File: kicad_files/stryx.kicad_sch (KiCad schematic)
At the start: 24 parts, among them M1 12V 250 RPM, M2 12V 250 RPM, U1 LM317_TO-220, U2 NUCLEO-L432KC, U3 TB6612FNG-Module, U4 HC-SR04

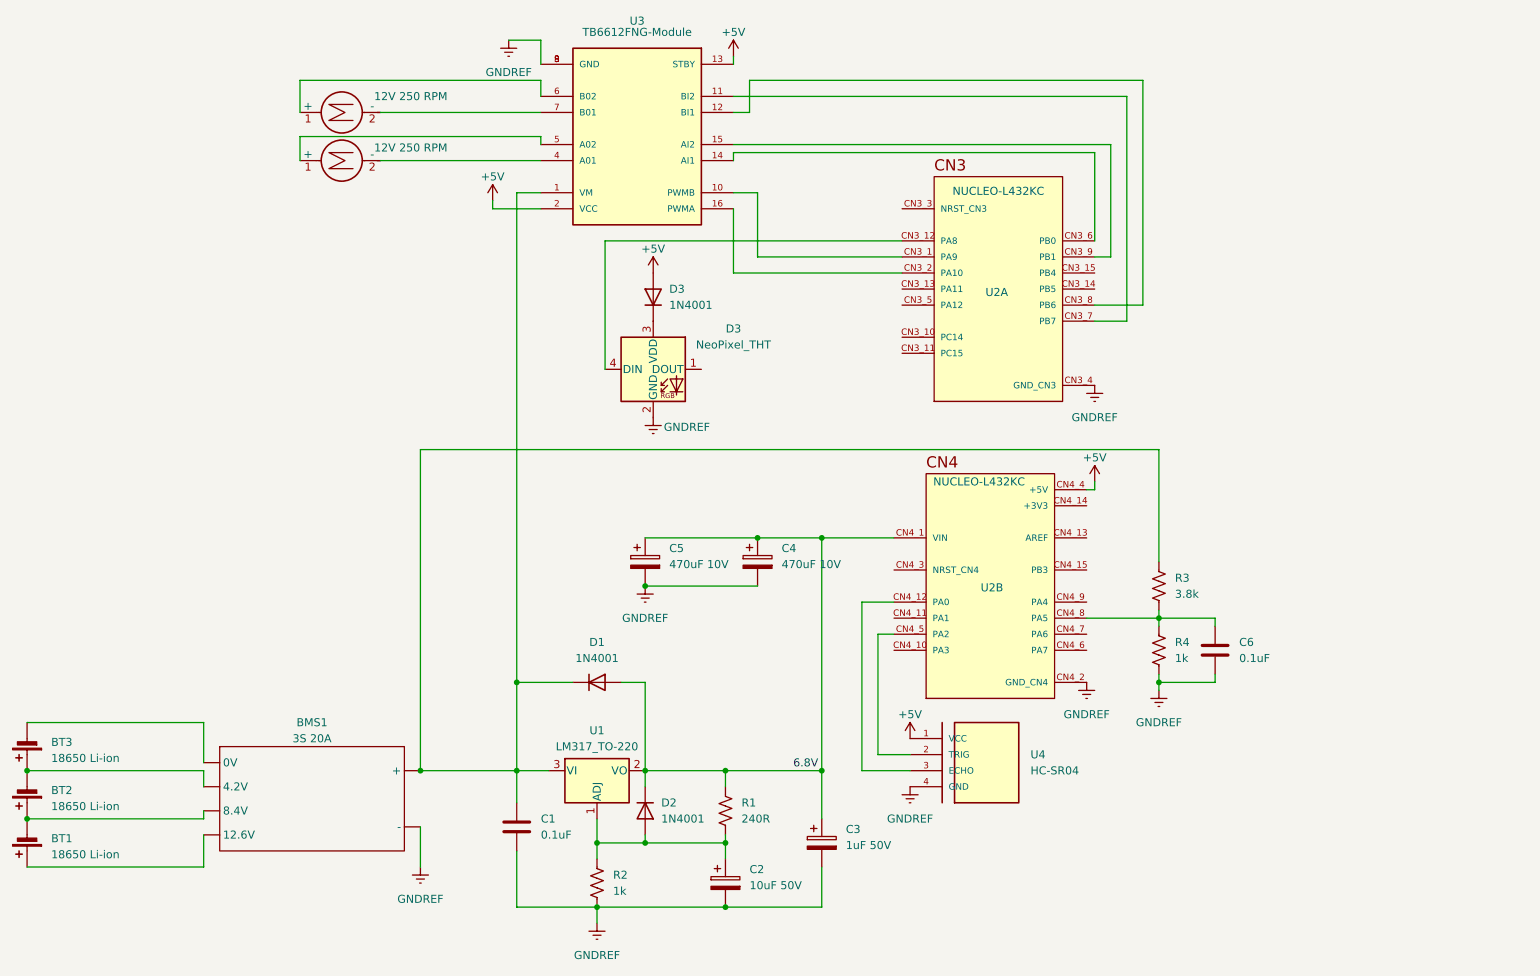
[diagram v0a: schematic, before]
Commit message: Updated schematic and deleted auto-generated backups. A future commit will disable tracking of backups
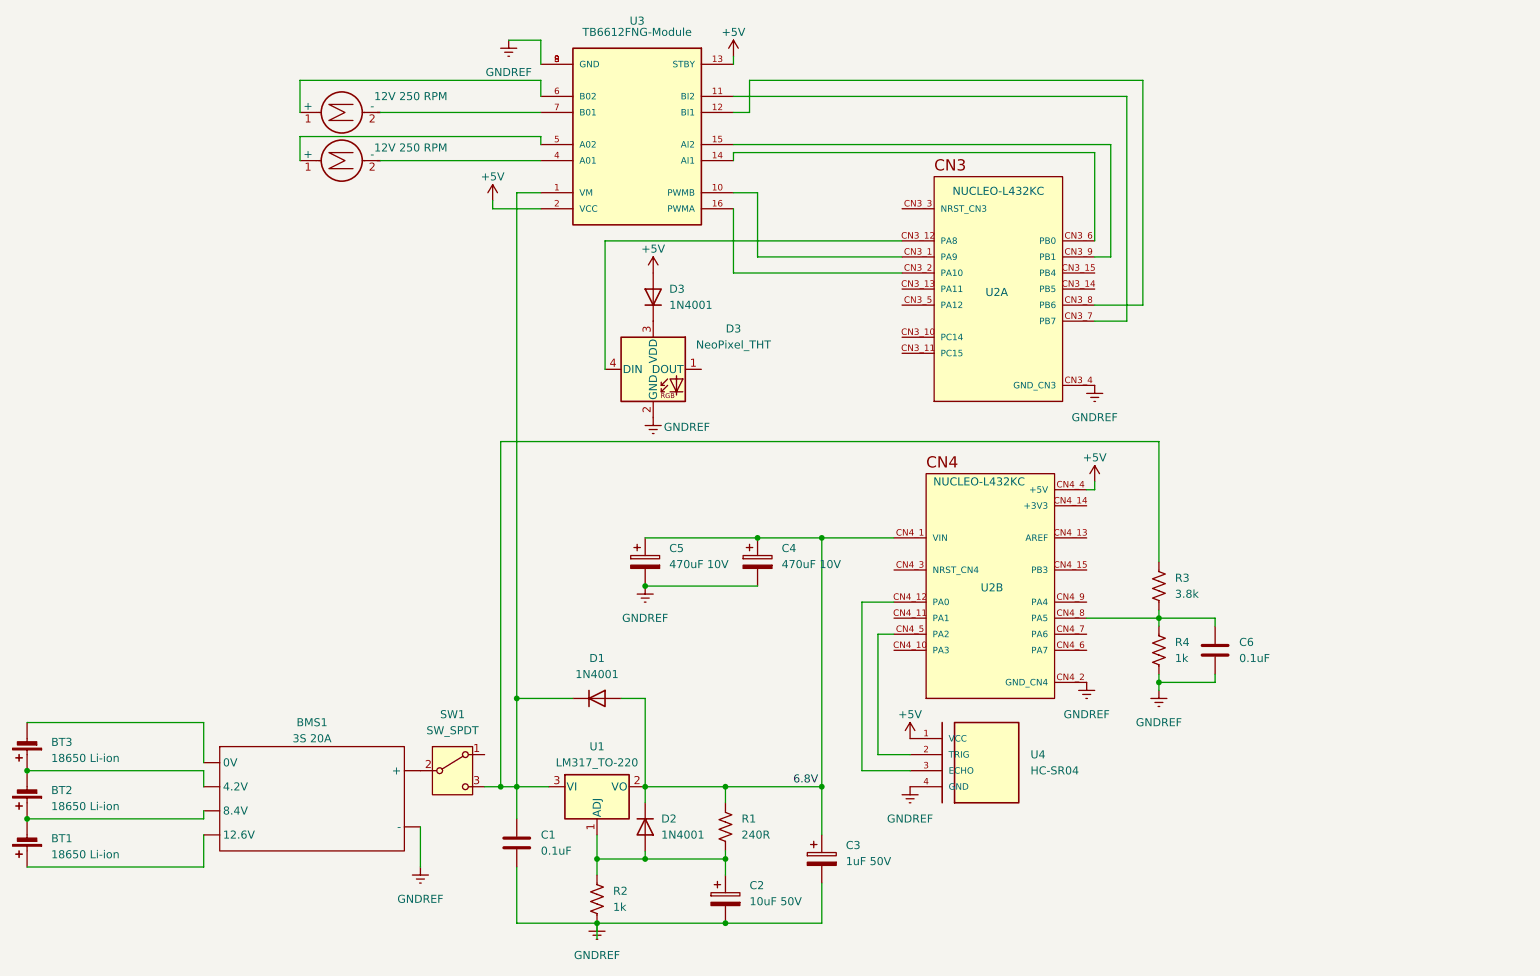
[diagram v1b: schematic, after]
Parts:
- added SW1: SW_SPDT, symbol Switch:SW_SPDT
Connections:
- net at C1.2, D1.1 (K), R3.1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: now also SW1.3 (C); no longer BMS1. (-)
- new net: BMS1. (-), SW1.2 (B)
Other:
- moved on the sheet: C1, C2, C3, D1, D2, R1, R2, U1

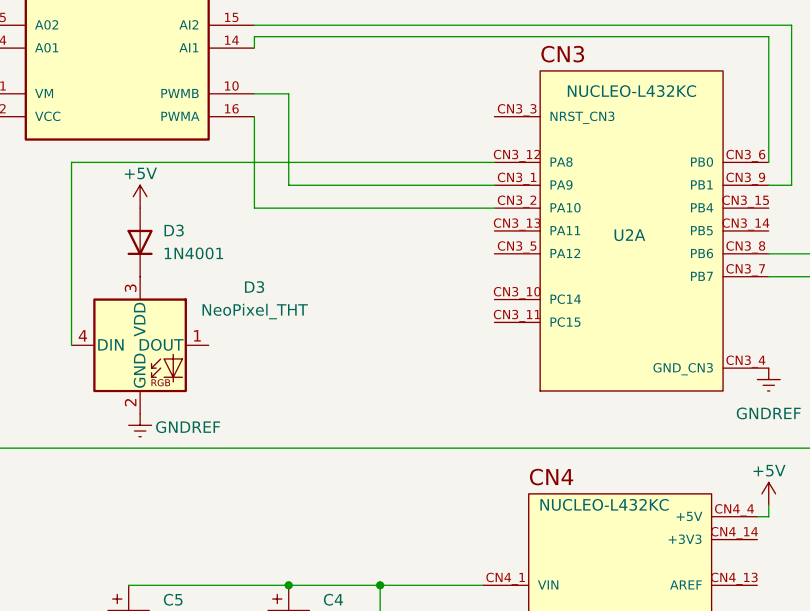
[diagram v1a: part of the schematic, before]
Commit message: Updated schematic to include USB connectivity
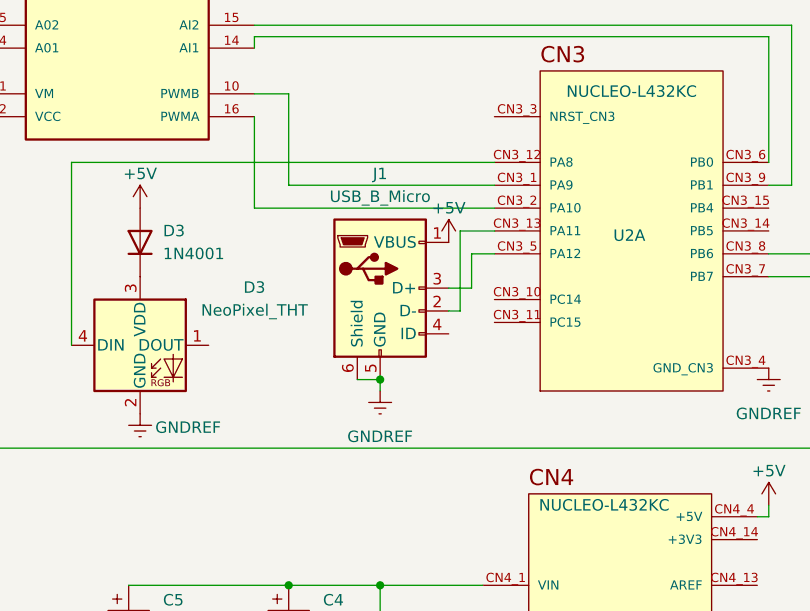
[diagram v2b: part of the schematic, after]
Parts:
- added J1: USB_B_Micro, symbol Connector:USB_B_Micro
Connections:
- net +5V: now also J1.1 (VBUS)
- net GNDREF: now also J1.5 (GND), J1.6 (Shield)
- net at U2.CN3_13 (PA11): now also J1.2 (D-)
- net at U2.CN3_5 (PA12): now also J1.3 (D+)

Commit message: Updated schematic
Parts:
- added U5: NRF24L01_Breakout, RF_Module:nRF24L01_Breakout, symbol RF:NRF24L01_Breakout
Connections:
- net GNDREF: now also U5.1 (GND)
- net at U2.CN3_14 (PB5): now also U5.6 (MOSI)
- net at U2.CN3_15 (PB4): now also U5.7 (MISO)
- net at U2.CN4_10 (PA3): now also U5.4 (~{CSN})
- net at U2.CN4_11 (PA1): now also U5.8 (IRQ)
- net +3V3: now reaches U2.CN4_14 (+3V3)
- net +3V3: now also U5.2 (VCC)
- net at U2.CN4_15 (PB3): now also U5.5 (SCK)
- net at U2.CN4_9 (PA4): now also U5.3 (CE)
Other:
- moved on the sheet: R3
